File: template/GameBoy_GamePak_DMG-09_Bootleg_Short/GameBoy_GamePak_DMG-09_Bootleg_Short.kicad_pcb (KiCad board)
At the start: 2 copper layers, 53 x 48.1 mm, 1 part, among them J1 GameBoy_GamePak_DMG-09

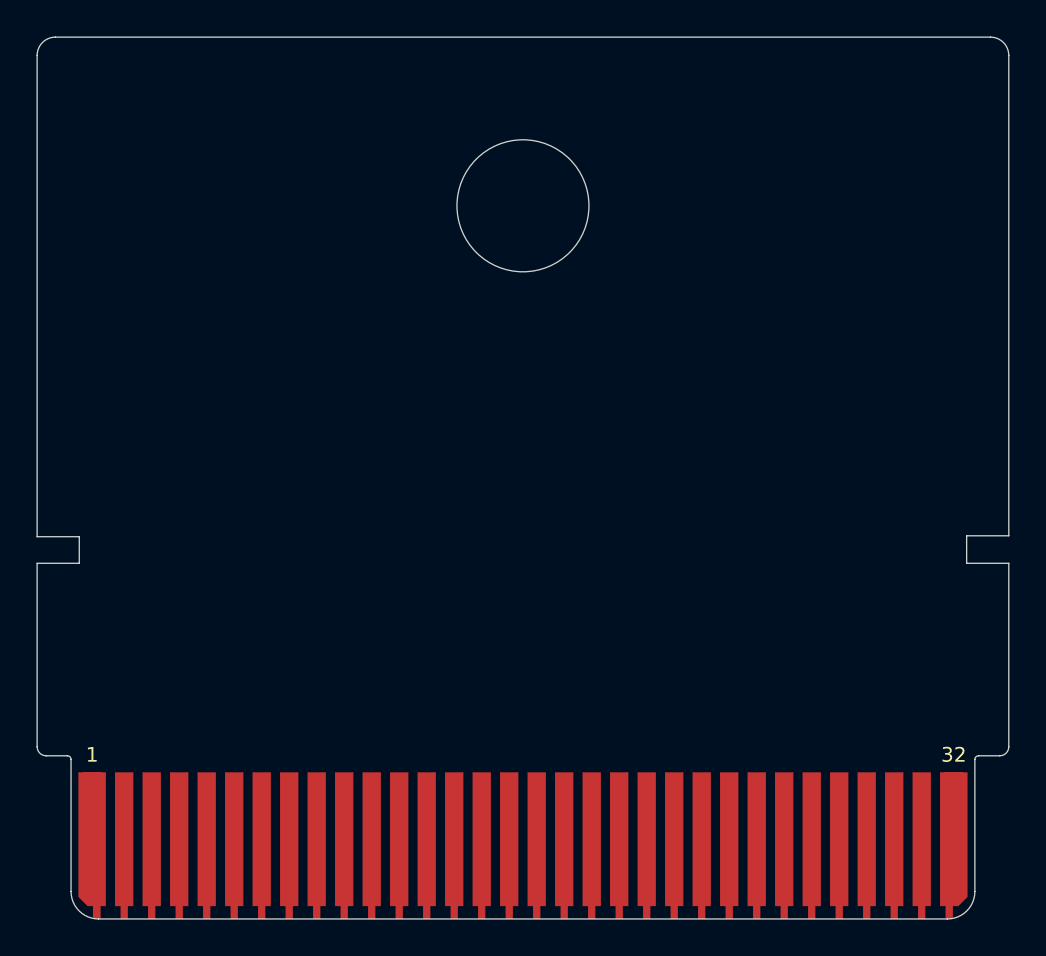
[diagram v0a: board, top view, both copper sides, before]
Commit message: Update all files to KiCAD 6.x format
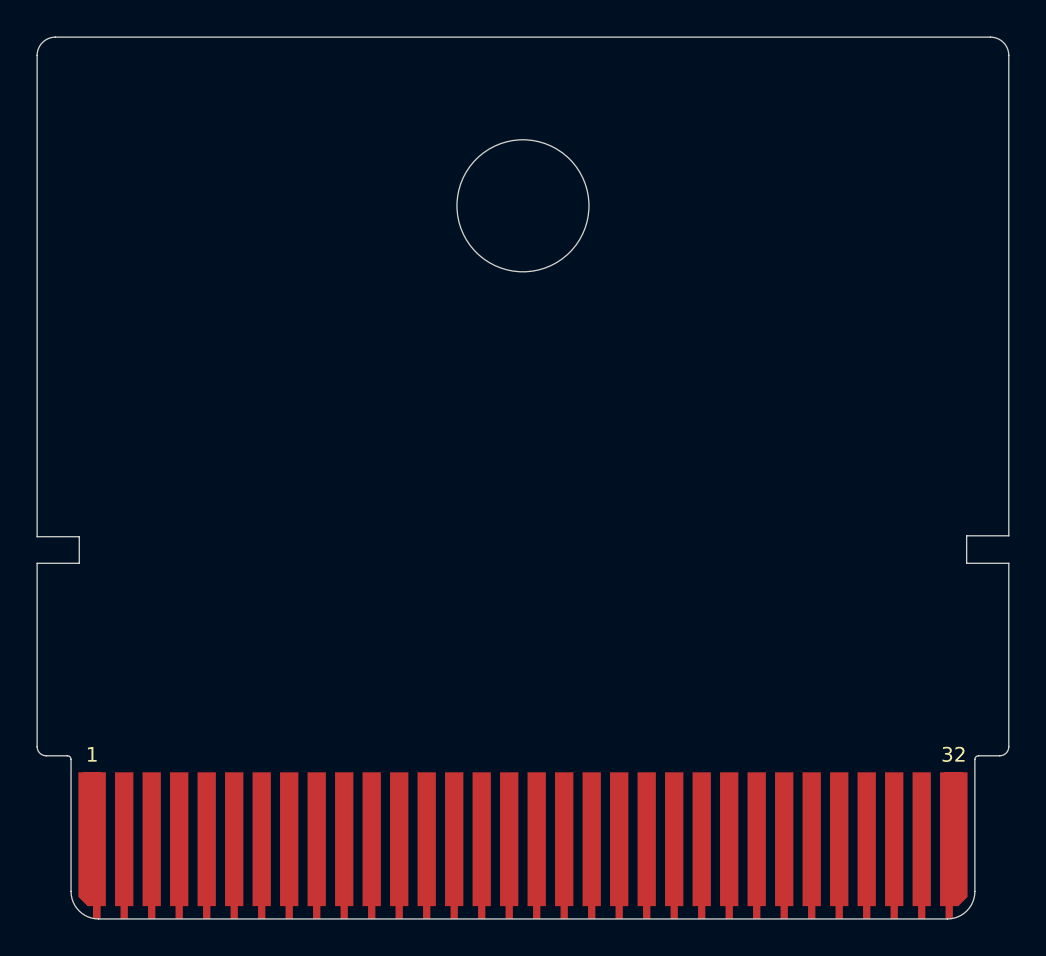
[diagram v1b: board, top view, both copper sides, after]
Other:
- net class Default removed
